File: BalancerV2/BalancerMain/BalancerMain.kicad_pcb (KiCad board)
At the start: 4 copper layers, 76 x 64 mm, 56 parts, among them J1 BATT 3S +/-, J2 BANNER bn/bu/wh, J3 MPU + / -, J4 GPS 3V3/GND/RX/TX, J6 ADXL357 P1, J7 ADXL357 P2, J8 DOCK pogo 5V/GND/DET, Q1 AO3400A, Q2 AO3401A, SW1 ACQUIRE, U1 FeatherS3[D], U2 TPS54202DDCR, U3 MT3608, U4 LM1815MX/NOPB

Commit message: v2 main unit: OMGS3 module on pads replaces the FeatherS3
Official Unexpected Maker symbol and footprint copied under
BalancerMain/vendor with their CERN OHL license. New GPIO map, PROG
header for USB D+/D-, IO0 and RESET, 5 V OR-ing diode removed. Board
regenerated with the module's antenna end at the board edge and the
LED moved off it. Pin map and design notes updated.

Co-Authored-By: Claude Fable 5.1 <noreply@anthropic.com>
Claude-Session: https://claude.ai/code/session_01XT5akMmBgbqYX83ryU4fFA
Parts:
- removed D1: SS14, Diode_SMD:D_SMA
- added J5: PROG GND/D-/D+/IO0/RST, Connector_PinHeader_2.54mm:PinHeader_1x05_P2.54mm_Vertical, F.Cu at (152.0, 118.0)
- U1: value FeatherS3[D] -> OMGS3; footprint BalancerMain:FeatherS3 -> BalancerMain:OMGS3
- moved LED1 26.0 mm to (170.0, 150.0)
- moved R20 26.0 mm to (170.0, 154.0)
- moved U1 4.12 mm to (148.0, 134.0), turned to 0 degrees
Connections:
- U1 pad 1: (no net) -> /GPS_UART_TX
- U1 pad 10: /DOCK_DET -> GND
- U1 pad 11: (no net) -> /PROG_RST
- U1 pad 12: (no net) -> +5V
- U1 pad 13: (no net) -> /PROG_IO0
- U1 pad 14: (no net) -> /USB_DM
- U1 pad 15: (no net) -> /USB_DP
- U1 pad 16: /STATUS_LED -> +3V3
- U1 pad 17: /OPT_TACH -> (no net)
- U1 pad 2: (no net) -> /GPS_UART_RX
- U1 pad 20: /BAT_SENSE -> /OPT_TACH
- U1 pad 21: /ACCEL_SCK -> /MAG_TACH
- U1 pad 22: /ACCEL_MISO -> /ACCEL_DRDY
- U1 pad 23: /ACCEL_DRDY -> (no net)
- U1 pad 24: /ACCEL_CS -> /STATUS_LED
- U1 pad 25: GND -> /ACCEL_CS
- U1 pad 3: /FEATHER_5V -> /BAT_SENSE
- U1 pad 4: /ACCEL_MOSI -> /DOCK_DET
- U1 pad 5: /GPS_UART_TX -> /BOOST_EN
- U1 pad 6: /GPS_UART_RX -> /ACCEL_SCK
- U1 pad 7: (no net) -> /ACCEL_MISO
- U1 pad 8: /MAG_TACH -> /ACCEL_MOSI
- U1 pad 9: /BOOST_EN -> (no net)
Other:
- board text added: "OMGS3 antenna: no copper, no ground pour"

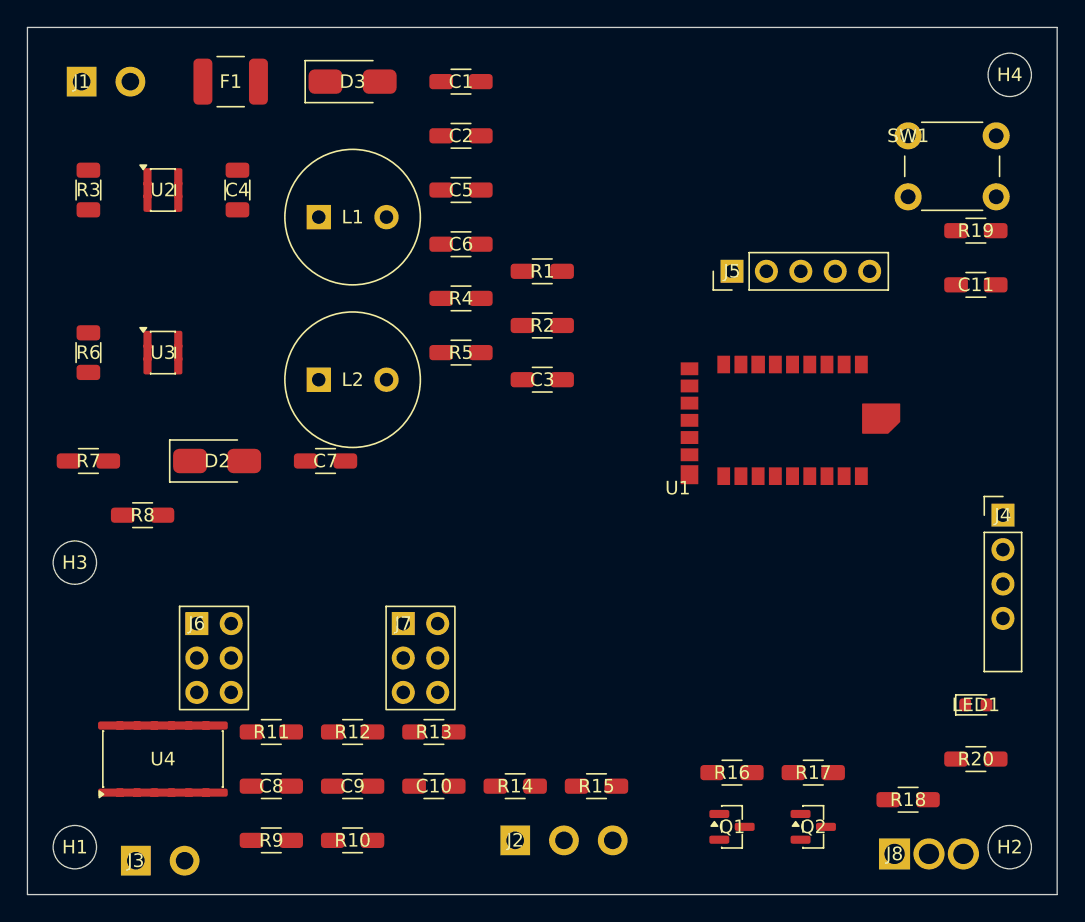
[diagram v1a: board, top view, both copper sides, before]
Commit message: v2 main unit: 1S LiPo on the OMGS3 charger, USB-C, 12 V boost only for the Banner
Removes the 3S input, buck, battery divider and dock switch. Adds JST-PH
cell connector, USB-C 16P (Unexpected Maker's footprint and wiring from
their OMGS3 carrier), CC resistors, VBUS Schottky, 1x03 IO0/RST header.
Board is 70 x 64 mm with 41 footprints; netlist check passes (33 nets).

Co-Authored-By: Claude Fable 5.1 <noreply@anthropic.com>
Claude-Session: https://claude.ai/code/session_01XT5akMmBgbqYX83ryU4fFA
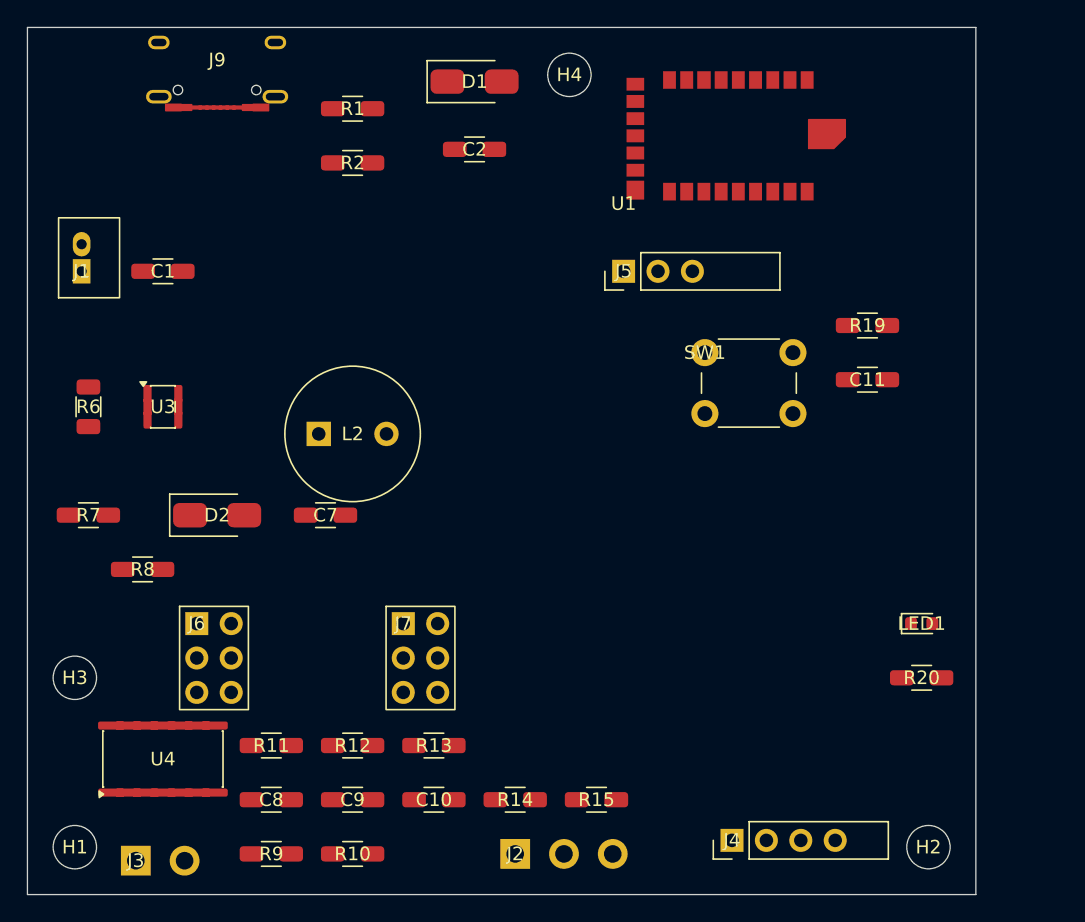
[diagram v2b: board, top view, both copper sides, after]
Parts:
- removed C3, C4: 100n, Capacitor_SMD:C_1206_3216Metric
- removed C5, C6: 10u 25V, Capacitor_SMD:C_1206_3216Metric
- removed D3: SS14, Diode_SMD:D_SMA
- removed F1: 2A polyfuse 1812, Fuse:Fuse_1812_4532Metric
- removed J8: DOCK pogo 5V/GND/DET, BalancerMain:Pogo_1x03
- removed L1: 10uH 3A, BalancerMain:L_Radial_D9_P5
- removed Q1: AO3400A, Package_TO_SOT_SMD:SOT-23
- removed Q2: AO3401A, Package_TO_SOT_SMD:SOT-23
- removed R16: 1k, Resistor_SMD:R_1206_3216Metric
- removed R17, R3: 100k, Resistor_SMD:R_1206_3216Metric
- removed R18, R5: 10k, Resistor_SMD:R_1206_3216Metric
- removed R4: 75k, Resistor_SMD:R_1206_3216Metric
- removed U2: TPS54202DDCR, Package_TO_SOT_SMD:SOT-23-6
- added D1: SS14, Diode_SMD:D_SMA, F.Cu at (133.0, 104.0)
- added J9: USB-C 16P, BalancerMain:USB_C_16P, F.Cu at (114.0, 102.4)
- J1: value BATT 3S +/- -> LIPO 1S JST-PH; footprint BalancerMain:SolderWire_1x02 -> BalancerMain:JST_PH_1x02_Vertical
- J5: value PROG GND/D-/D+/IO0/RST -> PROG GND/IO0/RST; footprint Connector_PinHeader_2.54mm:PinHeader_1x05_P2.54mm_Vertical -> Connector_PinHeader_2.54mm:PinHeader_1x03_P2.54mm_Vertical
- R1: value 100k -> 5.1k
- R2: value 10k -> 5.1k
- moved H4 32.5 mm to (140.0, 103.5)
- moved J4 31.2 mm to (152.0, 160.0), turned to 90 degrees
- moved C1 26.1 mm to (110.0, 118.0)
- moved SW1 21.9 mm to (150.0, 124.0)
- moved U1 21.4 mm to (144.0, 113.0)
- moved R1 18.4 mm to (124.0, 106.0)
- moved R2 18.4 mm to (124.0, 110.0)
- moved J1 14.0 mm to (104.0, 118.0), turned to 90 degrees
- moved C11 10.6 mm to (162.0, 126.0)
- moved R19 10.6 mm to (162.0, 122.0)
- moved H3 8.50 mm to (103.5, 148.0)
- moved J5 8.00 mm to (144.0, 118.0)
- moved LED1 7.21 mm to (166.0, 144.0)
- moved R20 7.21 mm to (166.0, 148.0)
- moved H2 6.00 mm to (166.5, 160.5)
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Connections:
- C2 pad 1: VBAT -> /MOD_5V
- J1 pad 1: /BAT_IN -> VBAT
- J5 pad 2: /USB_DM -> /PROG_IO0
- J5 pad 3: /USB_DP -> /PROG_RST
- R1 pad 1: VBAT -> /USB_CC1
- R1 pad 2: /BAT_SENSE -> GND
- R2 pad 1: /BAT_SENSE -> /USB_CC2
- U1 pad 12: +5V -> /MOD_5V
- U1 pad 17: (no net) -> VBAT
- U1 pad 18: /DOCK_EN -> (no net)
- U1 pad 3: /BAT_SENSE -> (no net)
- U1 pad 4: /DOCK_DET -> (no net)
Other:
- board size 76 x 64 mm -> 70 x 64 mm

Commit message: v2 main unit: status LED moved from IO8 to IO14, fuel-gauge I2C left free
Co-Authored-By: Claude Fable 5.1 <noreply@anthropic.com>
Claude-Session: https://claude.ai/code/session_01XT5akMmBgbqYX83ryU4fFA
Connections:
- U1 pad 18: (no net) -> /STATUS_LED
- U1 pad 24: /STATUS_LED -> (no net)
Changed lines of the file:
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@@
 			(size 0.95 1.3)
 			(layers "F.Cu" "F.Paste" "F.Mask")
+			(net "/STATUS_LED")
 		)
 		(pad "19" smd rect
@@
 			(size 0.95 1.3)
 			(layers "F.Cu" "F.Paste" "F.Mask")
-			(net "/STATUS_LED")
 		)
 		(pad "25" smd rect
